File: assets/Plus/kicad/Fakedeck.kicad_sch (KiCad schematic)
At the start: 9 parts, among them J1 Conn_01x06_Pin, J2 Conn_01x06_Pin, SW1 RotaryEncoder_Switch, SW2 RotaryEncoder_Switch, SW3 RotaryEncoder_Switch, SW4 RotaryEncoder_Switch, U1 Pico, U2 ATtiny2313-20P

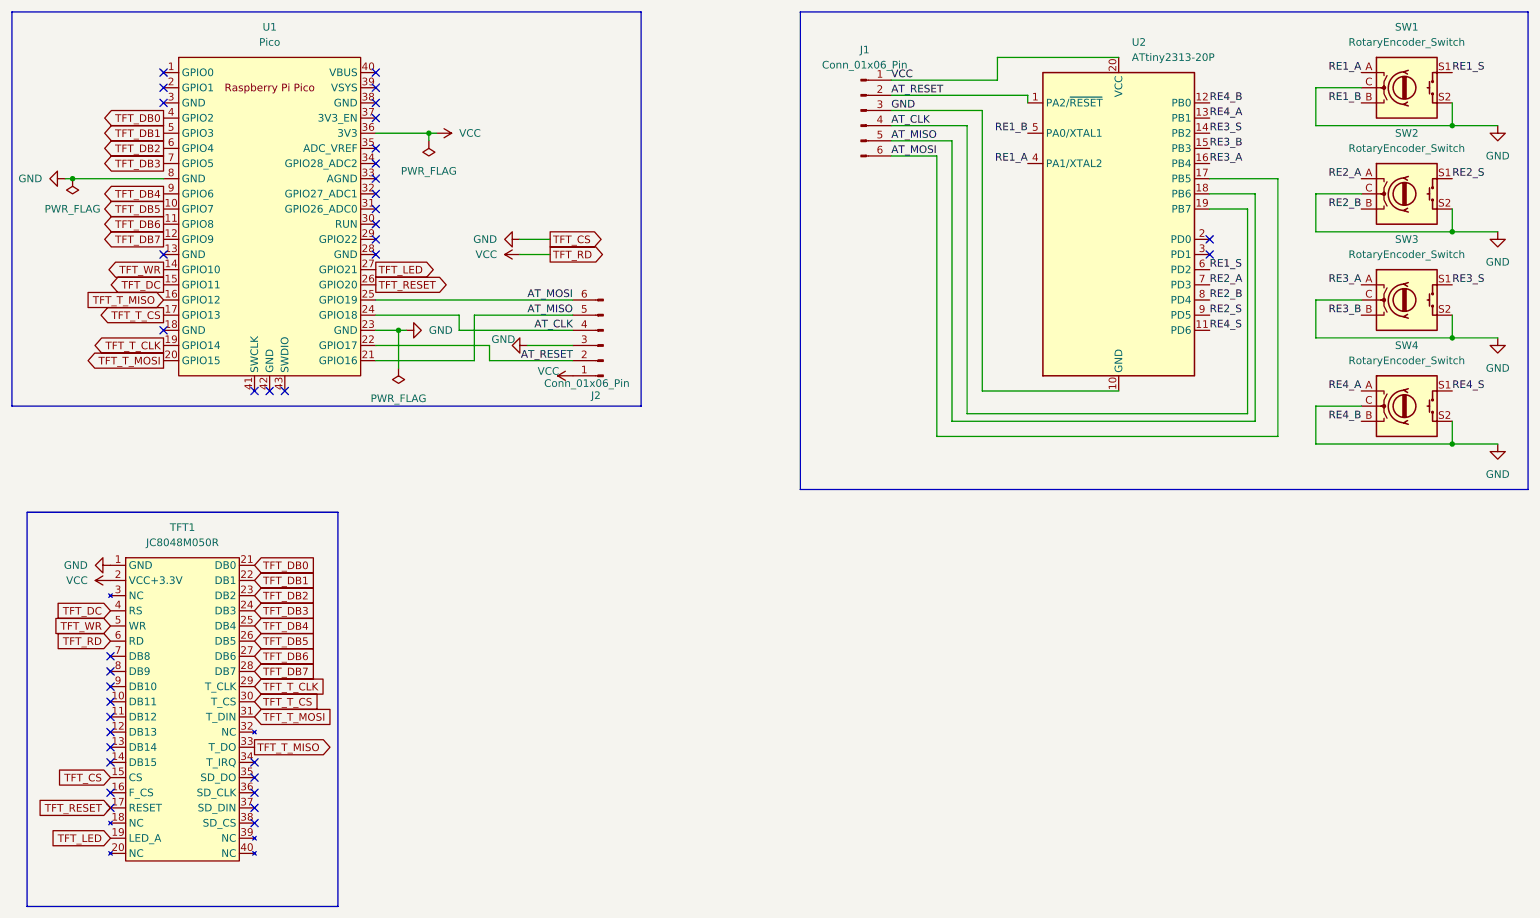
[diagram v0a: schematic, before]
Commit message: Plus: Changed to connect the rotary encoder directly to the Pico. Removed the Attiny. - Updated the PCB.
 Co-Authored-By: Claude Sonnet 4.6 <noreply@anthropic.com>
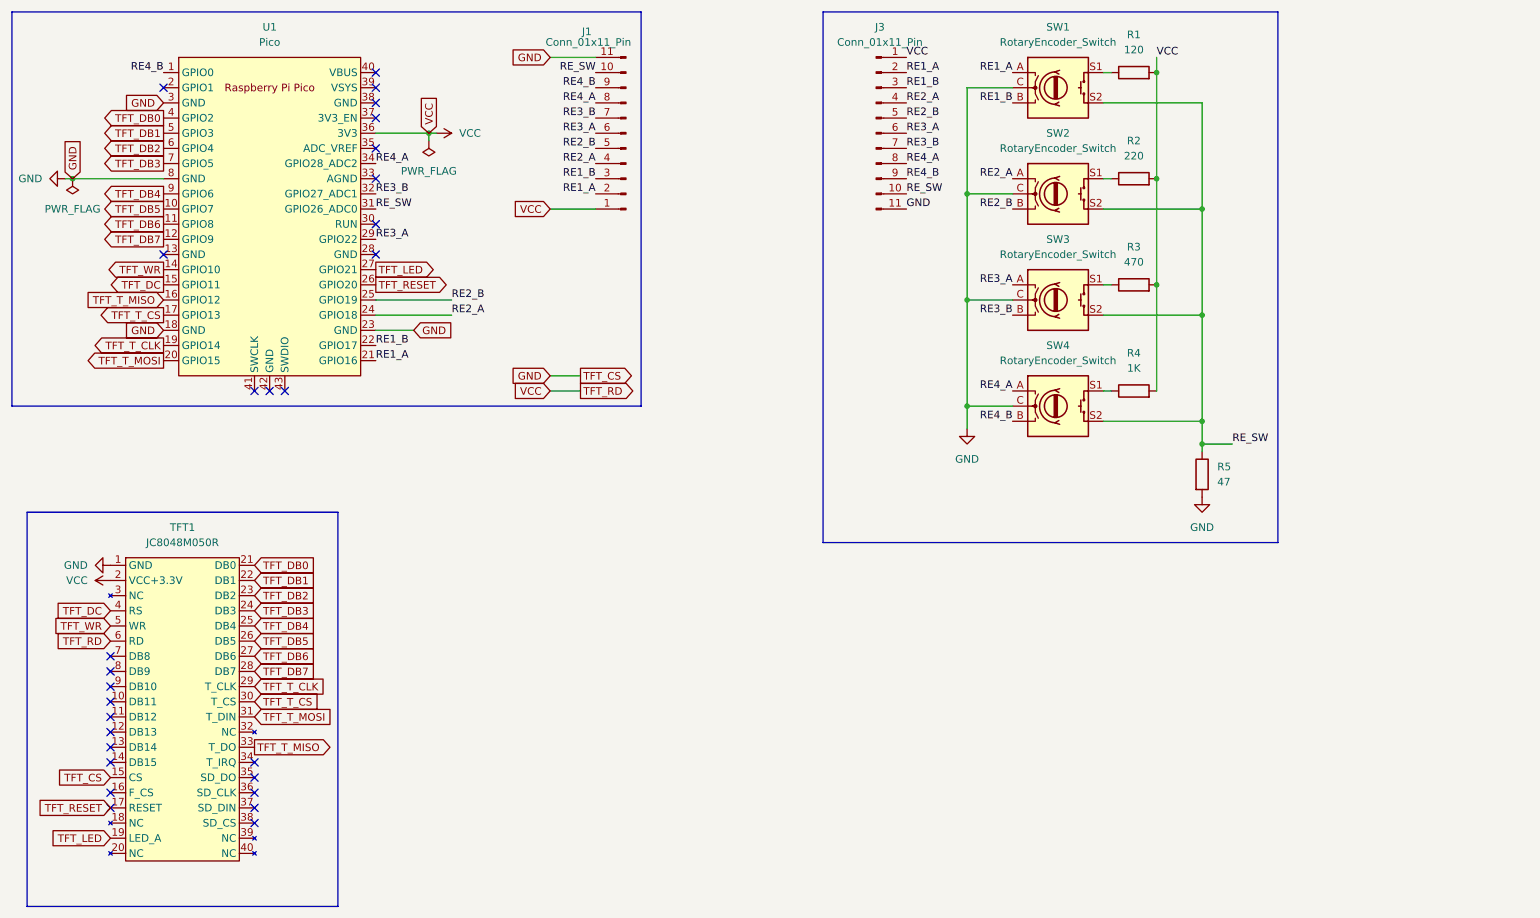
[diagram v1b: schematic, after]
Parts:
- removed J1, J2: Conn_01x06_Pin, Connector_Pin_2.54mm_Castellated:PinHeader_Castellated_1x06_P2.54mm_Vertical, symbol Connector:Conn_01x06_Pin
- removed U2: ATtiny2313-20P, Package_DIP:DIP-20_W7.62mm, symbol MCU_Microchip_ATtiny:ATtiny2313-20P
- added J1, J3: Conn_01x11_Pin, Connector_Pin_2.54mm_Castellated:PinHeader_Castellated_1x11_P2.54mm_Vertical, symbol Connector:Conn_01x11_Pin
- added R1: 120, Resistor_THT:R_Axial_DIN0207_L6.3mm_D2.5mm_P7.62mm_Horizontal, symbol Device:R
- added R2: 220, Resistor_THT:R_Axial_DIN0207_L6.3mm_D2.5mm_P7.62mm_Horizontal, symbol Device:R
- added R3: 470, Resistor_THT:R_Axial_DIN0207_L6.3mm_D2.5mm_P7.62mm_Horizontal, symbol Device:R
- added R4: 1K, Resistor_THT:R_Axial_DIN0207_L6.3mm_D2.5mm_P7.62mm_Horizontal, symbol Device:R
- added R5: 47, Resistor_THT:R_Axial_DIN0207_L6.3mm_D2.5mm_P7.62mm_Horizontal, symbol Device:R
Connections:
- net AT_CLK is gone; now on net RE2_A: U1.24 (GPIO18)
- net AT_MISO is gone; now on net RE1_A: U1.21 (GPIO16)
- net AT_MOSI is gone; now on net RE2_B: U1.25 (GPIO19)
- net AT_RESET is gone; now on net RE1_B: U1.22 (GPIO17)
- net GND: now also U1.18 (GND), U1.3 (GND), J1.11 (Pin_11), J3.11 (Pin_11), R5.2; no longer SW1.S2, SW2.S2, SW3.S2, SW4.S2
- net RE1_A: now also J1.2 (Pin_2), J3.2 (Pin_2)
- net RE1_B: now also J1.3 (Pin_3), J3.3 (Pin_3)
- net RE2_A: now also J1.4 (Pin_4), J3.4 (Pin_4)
- net RE2_B: now also J1.5 (Pin_5), J3.5 (Pin_5)
- net RE3_A: now also U1.29 (GPIO22), J1.6 (Pin_6), J3.6 (Pin_6)
- net RE3_B: now also U1.32 (GPIO27_ADC1), J1.7 (Pin_7), J3.7 (Pin_7)
- net RE4_A: now also U1.34 (GPIO28_ADC2), J1.8 (Pin_8), J3.8 (Pin_8)
- net RE4_B: now also U1.1 (GPIO0), J1.9 (Pin_9), J3.9 (Pin_9)
- net VCC: now also J1.1 (Pin_1), J3.1 (Pin_1), R1.2, R2.2, R3.2, R4.2
- net RE_SW: now reaches U1.31 (GPIO26_ADC0)
- net RE_SW: now also SW1.S2, SW2.S2, SW3.S2, SW4.S2, J1.10 (Pin_10), J3.10 (Pin_10), R5.1
- net RE1_S: no longer names the net of SW1.S1
- net RE1_S: now also R1.1
- net RE2_S: no longer names the net of SW2.S1
- net RE2_S: now also R2.1
- net RE3_S: no longer names the net of SW3.S1
- net RE3_S: now also R3.1
- net RE4_S: no longer names the net of SW4.S1
- net RE4_S: now also R4.1
- no-connect marks 37 -> 28
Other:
- moved on the sheet: SW1, SW2, SW3, SW4
